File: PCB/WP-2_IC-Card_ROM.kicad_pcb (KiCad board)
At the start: 2 copper layers, 54 x 54 mm, 11 parts, among them J1 SMS-138-01-G-S, SW1 Write-Enable, U1 29F0x0_TSOP

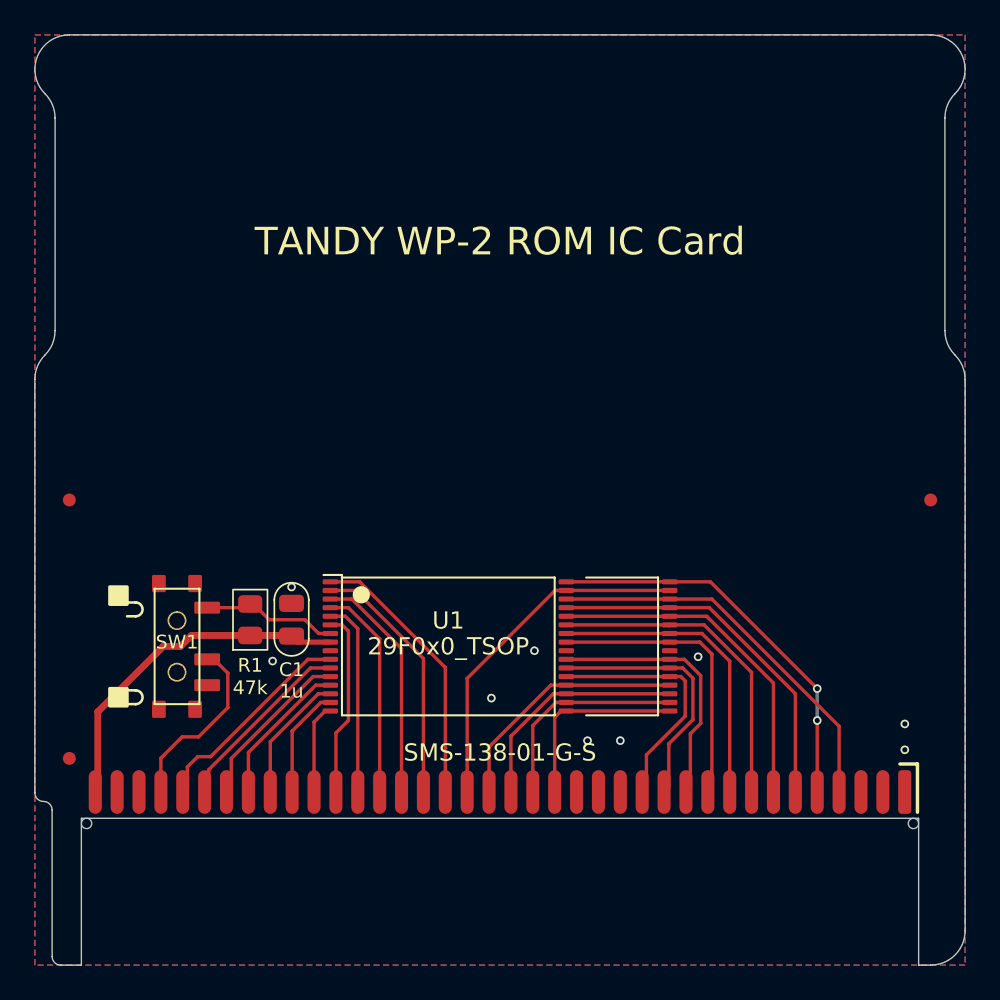
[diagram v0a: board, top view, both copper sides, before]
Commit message: update covers for flash & mram with bank sw & write sw
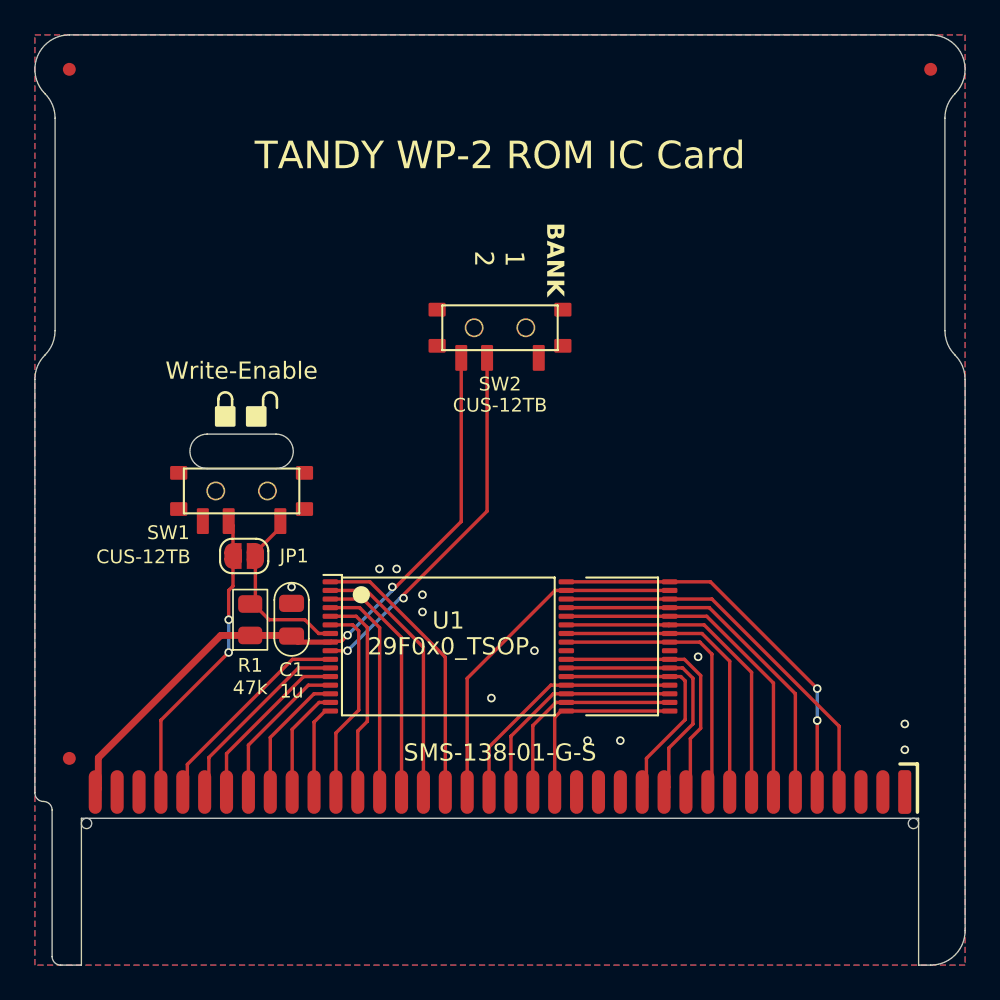
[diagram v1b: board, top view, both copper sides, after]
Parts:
- added JP1: WREN, 000_LOCAL:SolderJumper-2_open, F.Cu at (121.0, 102.9)
- added SW2: CUS-12TB, 000_LOCAL:CUS-12TB pth, F.Cu at (135.9, 89.7)
- N1: value WP-2_IC-Card_Cover_ROM -> WP-2_IC_Card_Cover_ROM
- SW1: value Write-Enable -> CUS-12TB; footprint 000_LOCAL:CUS-12TB pth -> 000_LOCAL:CUS-12TB slot pth
- moved REF** 25.0 mm to (110.9, 74.7)
- moved REF** 25.0 mm to (160.9, 74.7)
- moved SW1 9.77 mm to (120.9, 99.2), turned to 180 degrees
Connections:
- U1 pad 9: GND -> /A18
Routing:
- net /A18: track 0.00 -> 21.4 mm, vias 0 -> 2
- net VCC: track 20.2 -> 38.8 mm, vias 0 -> 2
- net /R~{W}: track 10.6 -> 17.6 mm, vias 0 -> 2
- net /~{WE}: track 7.95 -> 11.1 mm
- net /A7: track 10.8 -> 11.7 mm
- net /A8: track 11.4 -> 12.2 mm
- net GND: vias 9 -> 12
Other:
- board text added: "1 2"

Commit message: update pics
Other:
- board text added: "PCB THICKNESS 1.2mm"
- board text removed: "PCB thickness 1.2mm"
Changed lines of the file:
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@@
 		(at 135.89 89.695 180)
 		(property "Reference" "SW2"
-			(at 0 -3.275 360)
+			(at 0 -3.275 0)
 			(layer "F.SilkS")
 			(effects
@@
 		)
 		(property "Footprint" "000_LOCAL:CUS-12TB pth"
-			(at 0 0 360)
+			(at 0 0 0)
 			(layer "F.Fab")
 			(hide yes)
@@
 		)
 		(property "Datasheet" "datasheets/cus.pdf"
-			(at 0 0 360)
+			(at 0 0 0)
 			(layer "F.Fab")
 			(hide yes)
@@
 		)
 		(property "Description" "Switch, 2 position, single pole 2 throw, 2 position switch, SPDT"
-			(at 0 0 360)
+			(at 0 0 0)
 			(layer "F.Fab")
 			(hide yes)
@@
 		)
 		(property "LABEL" "BANK"
-			(at -3.2 3.95 270)
+			(at -3.2 3.95 -90)
 			(unlocked yes)
 			(layer "F.SilkS")
@@
 		(fp_arc
 			(start 25.828427 -22.171574)
-			(mid 25.980661 -22.936945)
+			(mid 25.980667 -22.936939)
 			(end 26.414213 -23.585788)
 			(stroke
@@
 		(fp_arc
 			(start 26.414214 -8.414214)
-			(mid 25.980662 -9.063056)
+			(mid 25.98065 -9.063055)
 			(end 25.828427 -9.828428)
 			(stroke
@@
 		)
 	)
-	(gr_text "PCB thickness 1.2mm"
-		(at 135.89 67.195 0)
+	(gr_text "PCB THICKNESS 1.2mm"
+		(at 135.89 69.695 0)
 		(layer "Eco1.User")
 		(effects

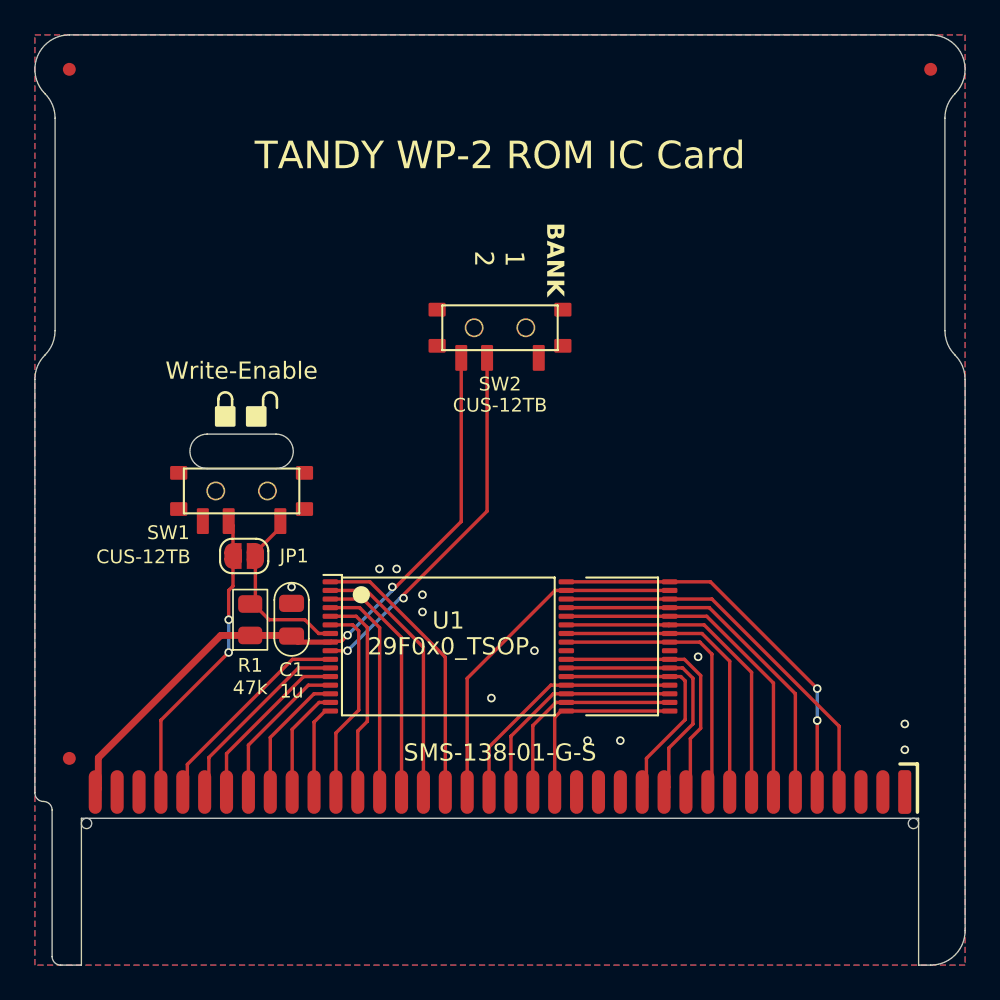
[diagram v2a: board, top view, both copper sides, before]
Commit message: add resistor for A18 on rom card
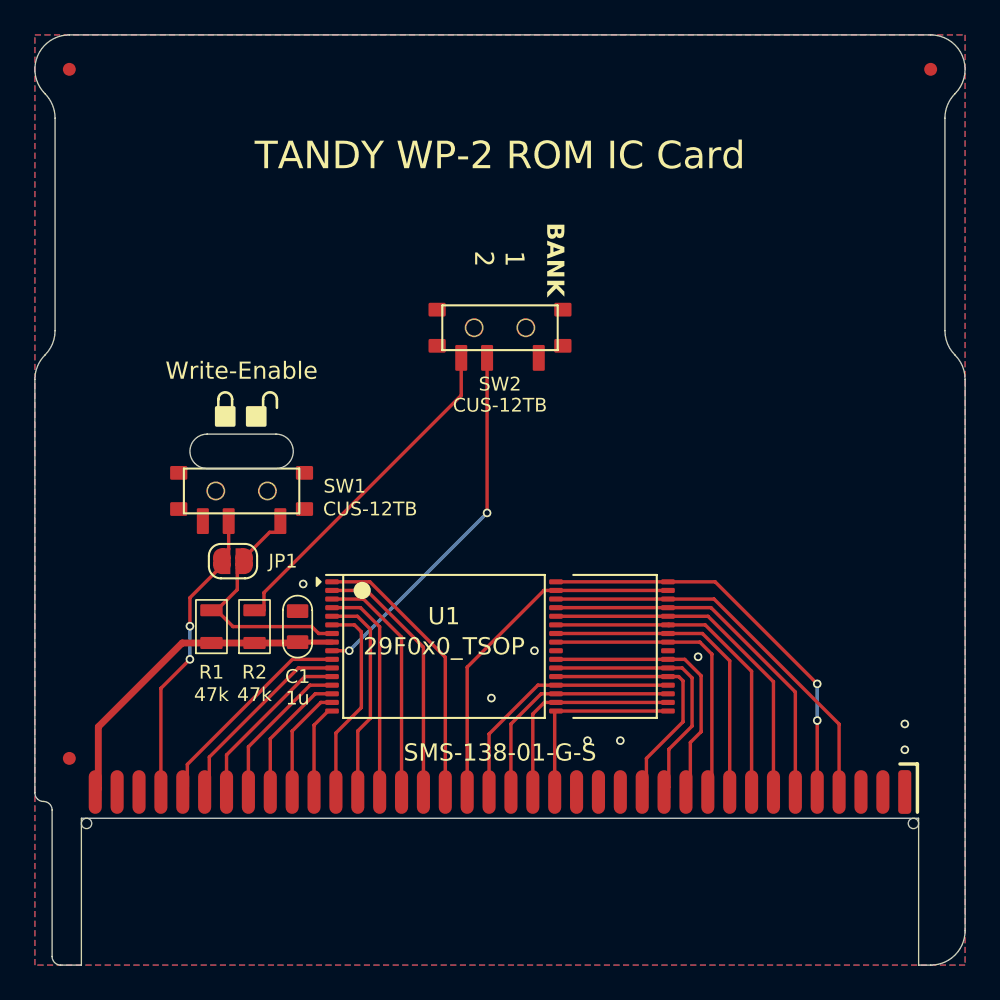
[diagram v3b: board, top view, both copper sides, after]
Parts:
- added R2: 47k, 000_LOCAL:R_0805, F.Cu at (121.6, 107.0)
- N1: value WP-2_IC_Card_Cover_ROM -> WP-2_IC-Card_Cover_ROM
- moved U1 3.25 mm to (132.6, 108.2)
- moved R1 2.29 mm to (119.1, 107.0)
- moved JP1 0.72 mm to (120.4, 103.2)
- moved C1 0.53 mm to (124.1, 107.0)
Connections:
- SW2 pad 3: VCC -> Net-(R2-Pad2)
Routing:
- net Net-(R2-Pad2): track 0.00 -> 19.9 mm
- net VCC: track 38.8 -> 19.5 mm, vias 2 -> 0
- net /~{WE}: track 11.1 -> 15.1 mm
- net /D2: track 18.9 -> 19.7 mm
- net /~{OE}: track 23.1 -> 23.9 mm
- net /~{CE}: track 22.7 -> 23.4 mm
- net /D0: track 21.1 -> 21.7 mm
- net /D1: track 19.9 -> 20.5 mm
- net /D5: track 15.3 -> 15.9 mm
- net /D3: track 18.7 -> 19.3 mm
- net /D4: track 16.8 -> 17.4 mm
- net /D6: track 14.9 -> 15.4 mm
- net GND: vias 12 -> 8

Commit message: SRAM compatible with 512K, pullup /WE, TSOP32 footprint, cfg jumpers
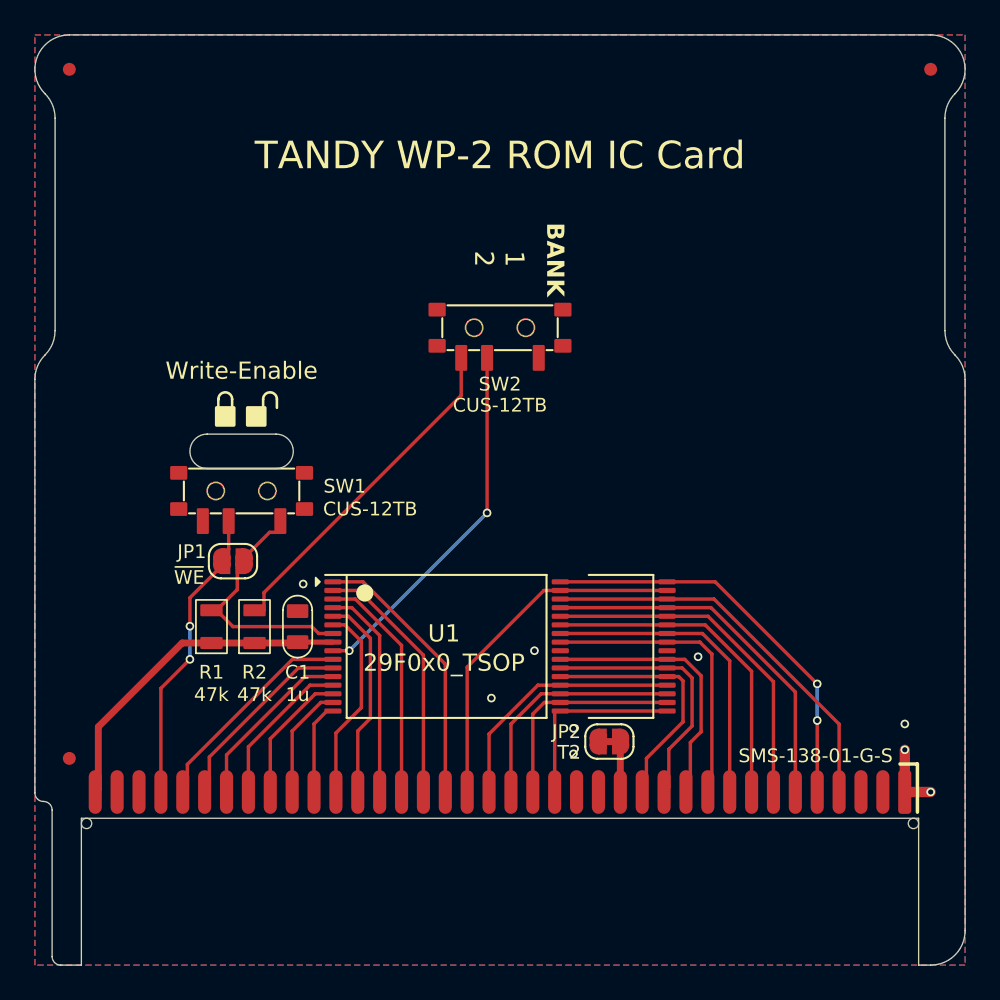
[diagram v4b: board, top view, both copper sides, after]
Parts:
- added JP2: T2, 000_LOCAL:SolderJumper-2_P1.3mm_Bridged_RoundedPad1.0x1.5mm, F.Cu at (142.2, 113.7)
- JP1: value WREN -> ~{WE}
- moved U1 3.25 mm to (135.9, 108.2)
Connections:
- J1 pad 14: GND -> /T2
- J1 pad 15: unconnected-(J1-Pin_15-Pad15) -> /S1
- J1 pad 16: unconnected-(J1-Pin_16-Pad16) -> /S2
- J1 pad 2: unconnected-(J1-Pin_2-Pad2) -> /~{DET}
- J1 pad 3: unconnected-(J1-Pin_3-Pad3) -> /CE2
- J1 pad 36: unconnected-(J1-Pin_36-Pad36) -> /S3
- J1 pad 37: unconnected-(J1-Pin_37-Pad37) -> /BCHK
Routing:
- net GND: track 0.00 -> 3.96 mm, vias 8 -> 9
- net /T2: track 0.00 -> 2.94 mm

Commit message: refactor cover scad more, cover models makefile, adjust new sram switch & batt positions
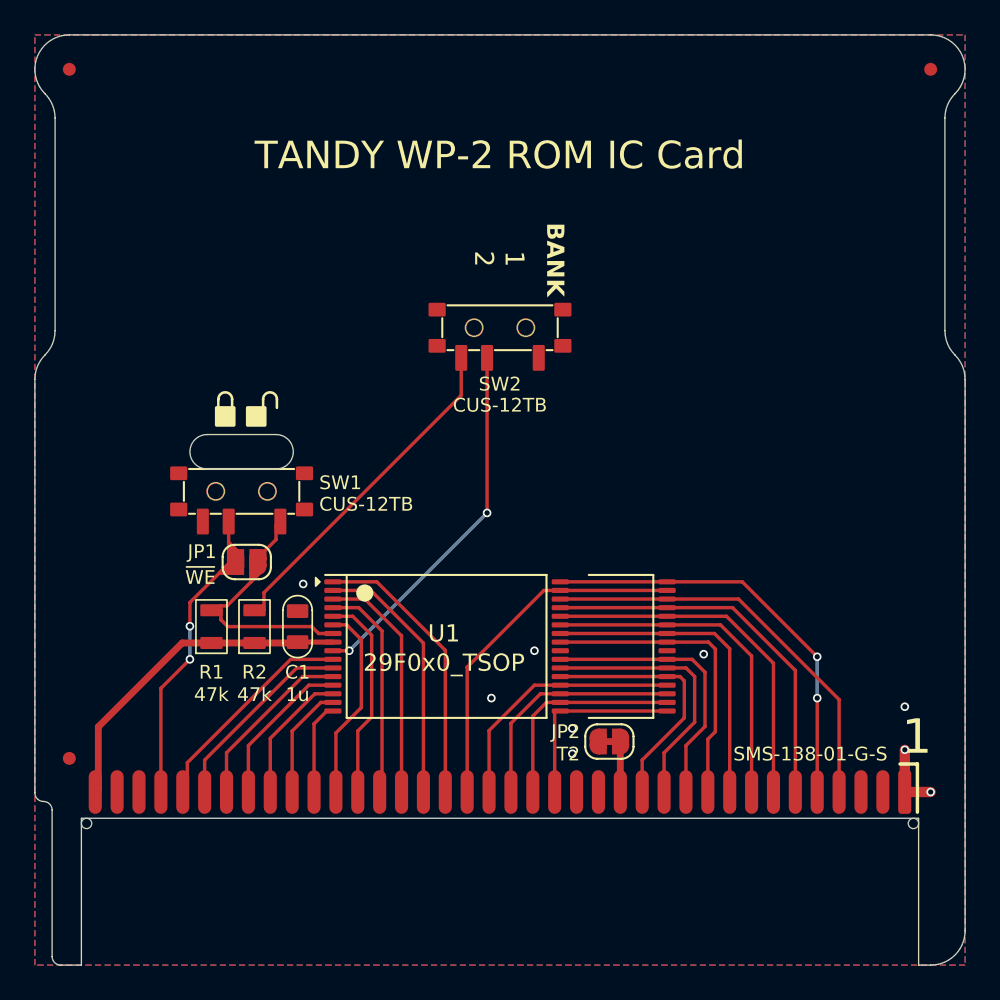
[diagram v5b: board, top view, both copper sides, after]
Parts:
- moved JP1 0.80 mm to (121.2, 103.3)
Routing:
- net /~{OE}: track 23.6 -> 24.6 mm
- net /~{CE}: track 23.1 -> 24.0 mm
- net /D0: track 21.5 -> 22.2 mm
- net /D1: track 20.4 -> 21.0 mm
- net /D2: track 19.2 -> 19.7 mm
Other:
- board text removed: "38"

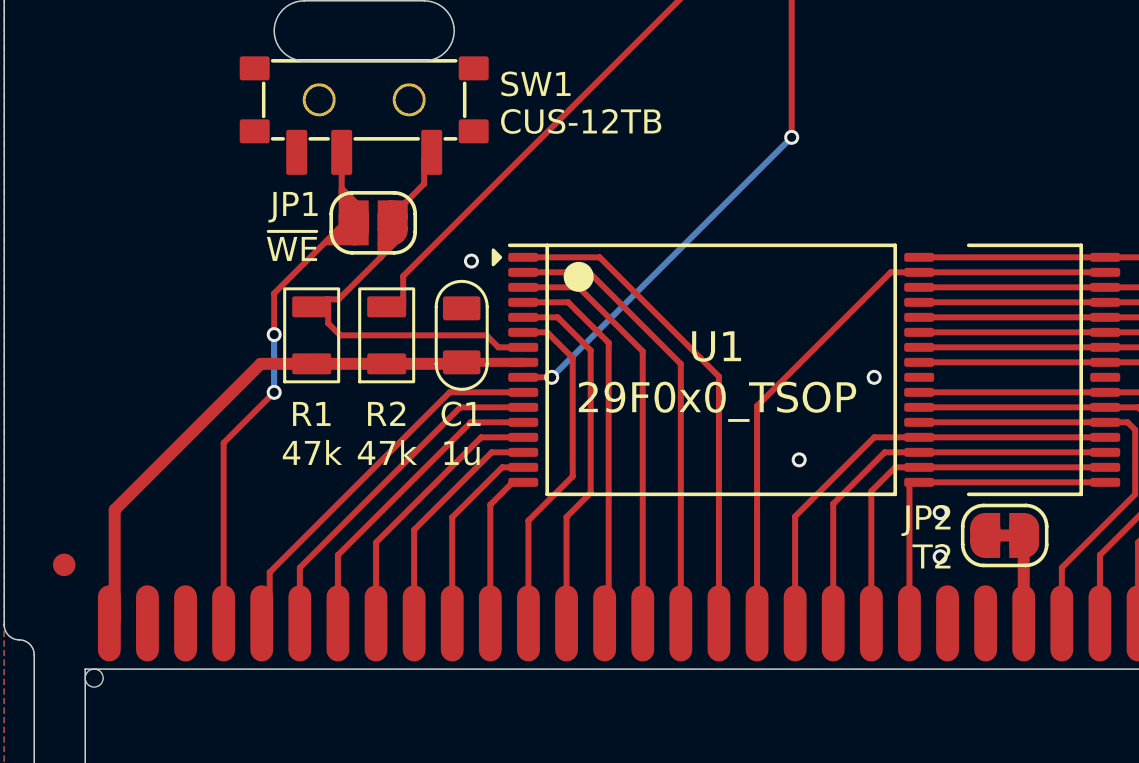
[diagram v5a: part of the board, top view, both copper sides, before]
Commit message: rom solder jumper footprints & pics
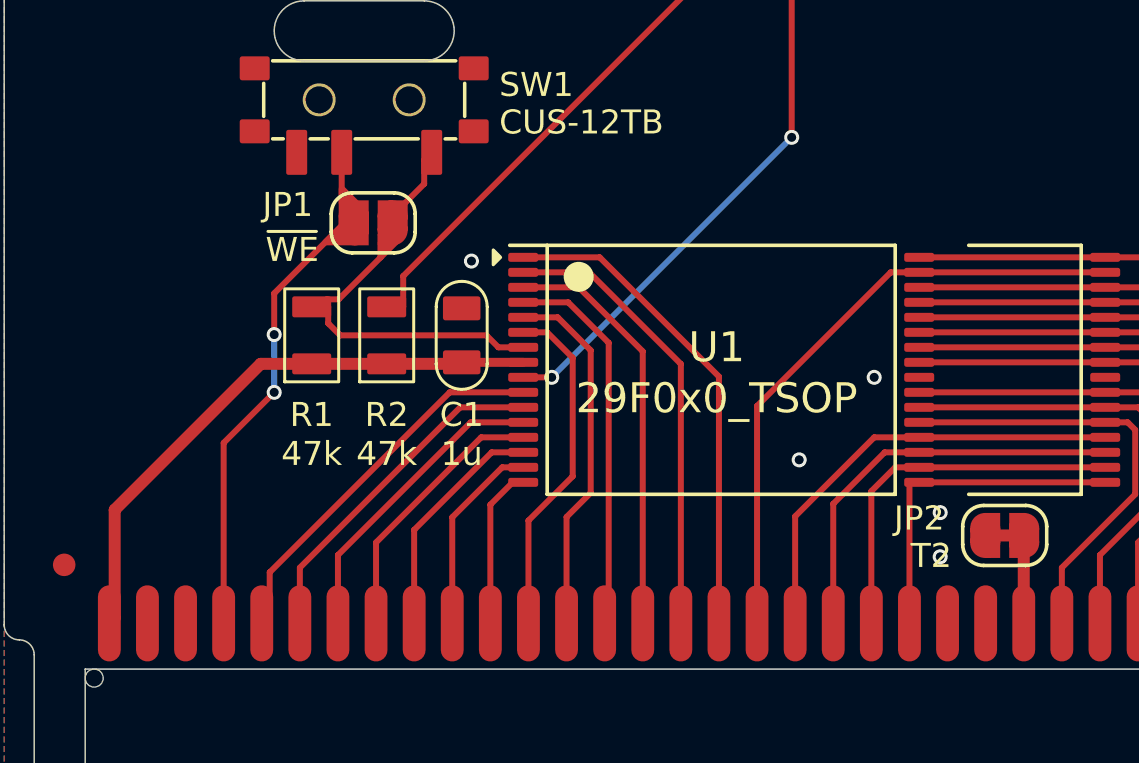
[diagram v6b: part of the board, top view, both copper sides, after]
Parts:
- JP2: footprint 000_LOCAL:SolderJumper-2_P1.3mm_Bridged_RoundedPad1.0x1.5mm -> 000_LOCAL:SolderJumper-2_Bridged

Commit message: renders
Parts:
- moved REF** 0.50 mm to (110.4, 114.7)
